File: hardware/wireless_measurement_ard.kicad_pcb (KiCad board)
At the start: 2 copper layers, 30 x 23 mm, 24 parts, among them J1 Conn_01x08, J2 Tag-Connect, SW1 SW_SPDT, U1 EFM8LB1, U2 JDY-08, U3 MCP16415, U4 MAX40204

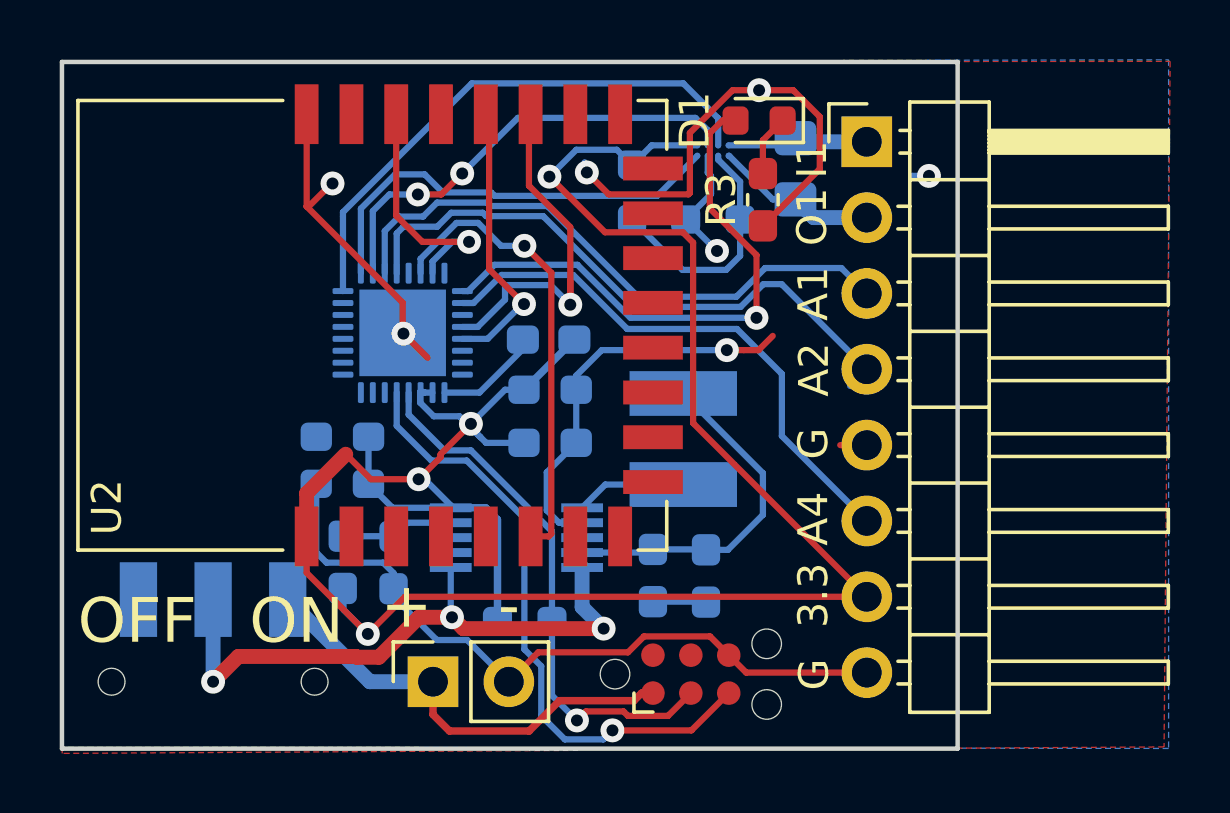
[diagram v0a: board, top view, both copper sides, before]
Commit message: critical fix for cap connectd to power instead of gnd
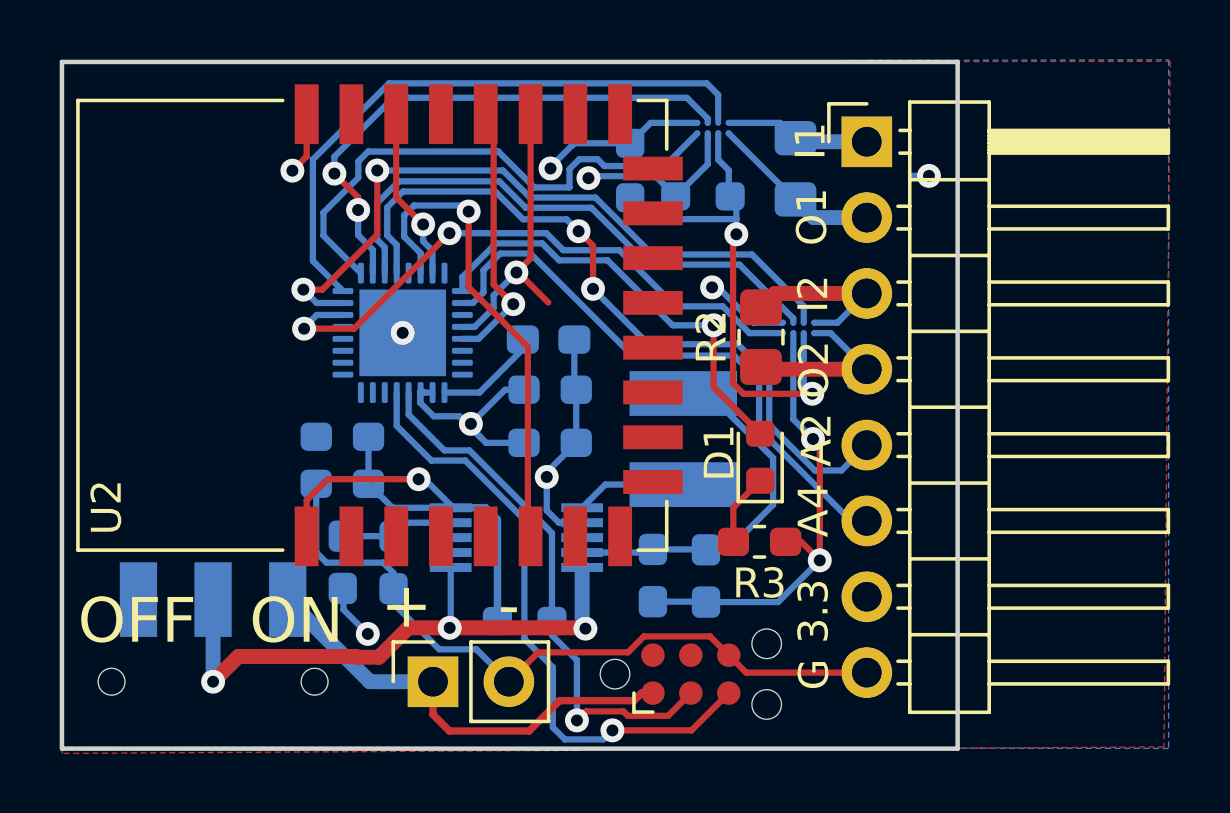
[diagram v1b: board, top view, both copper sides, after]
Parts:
- added R2: 1R, Resistor_SMD:R_0805_2012Metric_Pad1.20x1.40mm_HandSolder, F.Cu at (133.4, 84.2)
- added U5: MAX40204, ben_common:BGA-8_4x2_1.468x0.848mm, B.Cu at (134.7, 83.9)
- moved R3 11.5 mm to (133.4, 91.1), turned to 0 degrees
- moved D1 11.3 mm to (133.4, 88.2), turned to 90 degrees
- moved R8 0.84 mm to (131.5, 79.5)
- moved U4 0.75 mm to (131.8, 77.2)
- moved R7 0.73 mm to (129.0, 78.6)
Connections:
- net Net-(R7-Pad2) renamed HALF
- C7 pad 1: +3V3 -> GND
- J1 pad 3: A1 -> C2_IN
- J1 pad 4: A2 -> C2_OUT
- J1 pad 5: VHIGH -> A2
- U1 pad 14: Net-(U1-Pad14) -> MAX_SHDN2
- U1 pad 15: Net-(U1-Pad15) -> GAIN2
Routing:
- net +3V3: track 79.3 -> 35.0 mm, vias 4 -> 5
- net GAIN2: track 0.00 -> 23.6 mm, vias 0 -> 2
- net MAX_SHDN2: track 0.00 -> 20.3 mm, vias 0 -> 2
- net GND: track 71.2 -> 56.1 mm
- net HALF: track 8.17 -> 17.6 mm, vias 0 -> 2
- net C2_OUT: track 0.00 -> 6.57 mm
- net C2_IN: track 0.00 -> 5.90 mm
- net LED: track 18.8 -> 14.8 mm
- net A2: track 20.9 -> 24.7 mm, vias 0 -> 2
- net MAX_SHDN: track 14.8 -> 18.0 mm
- net A0: track 15.3 -> 18.2 mm
- net ARD_RX: track 12.5 -> 9.79 mm
- net PWRC: track 8.09 -> 5.83 mm
- net GAIN: track 18.4 -> 20.5 mm
- net STATUS: track 15.5 -> 16.8 mm
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- added copper zone on PWR, net +3V3
- added copper zone on GND, net GND
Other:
- copper layers 2 -> 4
- board text added: "I2"
- board text added: "O2"
- board text added: "SWM-mini-4 Oct 21"
- board text removed: "A1"
- board text removed: "SWM-mini-3 Oct 21"

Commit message: added logo
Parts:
- added U6: Logo, icons:icon, F.Cu at (114.8, 86.4)
- SW1: footprint Button_Switch_SMD:SW_SPDT_CK-JS102011SAQN -> ben_common:SW_SPDT_CK-JS102011SAQN

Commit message: update PCB
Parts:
- added C8: 4.7uF, Capacitor_SMD:C_0603_1608Metric_Pad1.08x0.95mm_HandSolder, F.Cu at (132.5, 77.1)
- added C9: 0.1uF, Capacitor_SMD:C_0603_1608Metric_Pad1.08x0.95mm_HandSolder, F.Cu at (132.5, 80.6)
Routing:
- net +3V3: track 35.0 -> 44.5 mm, vias 5 -> 6
- net GND: track 56.1 -> 60.2 mm, vias 7 -> 8
- net HALF: track 17.6 -> 19.1 mm

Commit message: Added capacitor
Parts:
- moved C8 0.99 mm to (133.5, 76.9)
- moved C9 0.97 mm to (133.5, 80.6)
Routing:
- net GND: track 60.2 -> 58.4 mm
- net +3V3: track 44.5 -> 46.1 mm
- net HALF: track 19.1 -> 17.6 mm

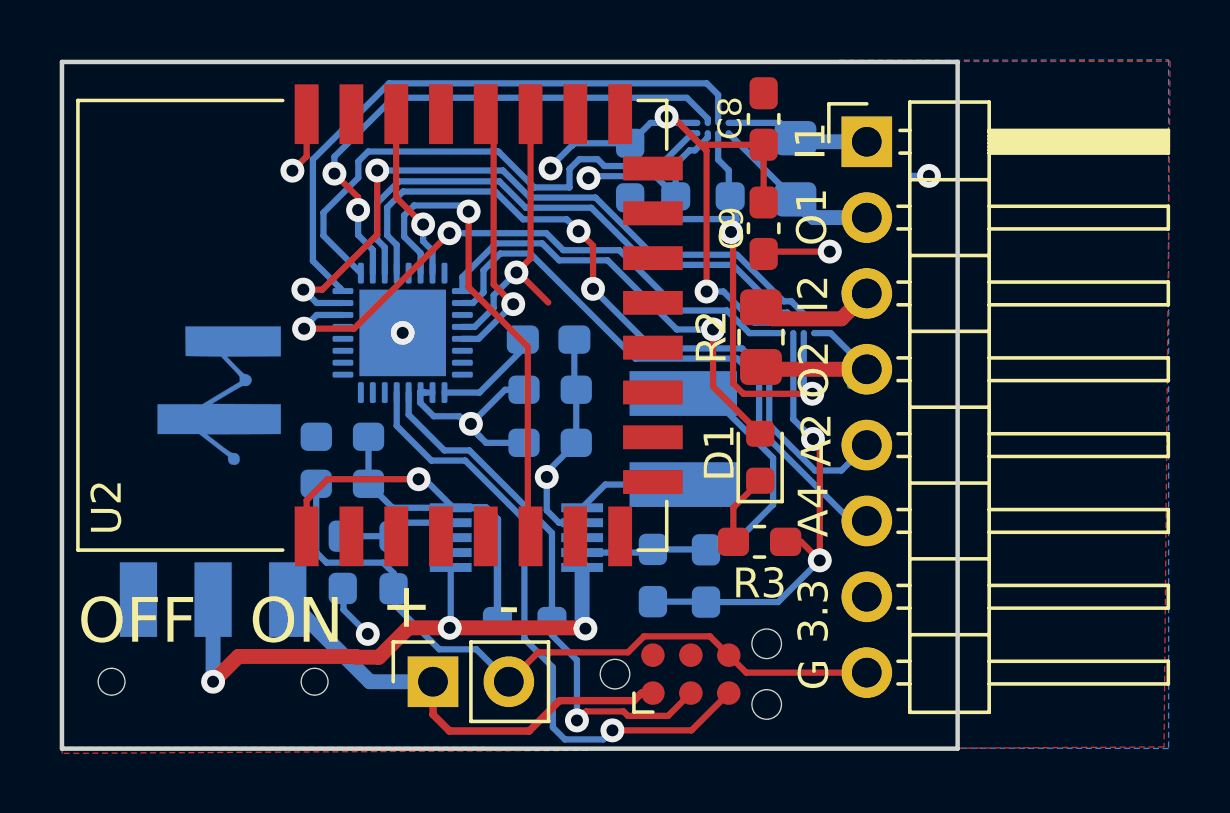
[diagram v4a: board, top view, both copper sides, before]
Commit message: added line to measure the half voltage for the MAX40204
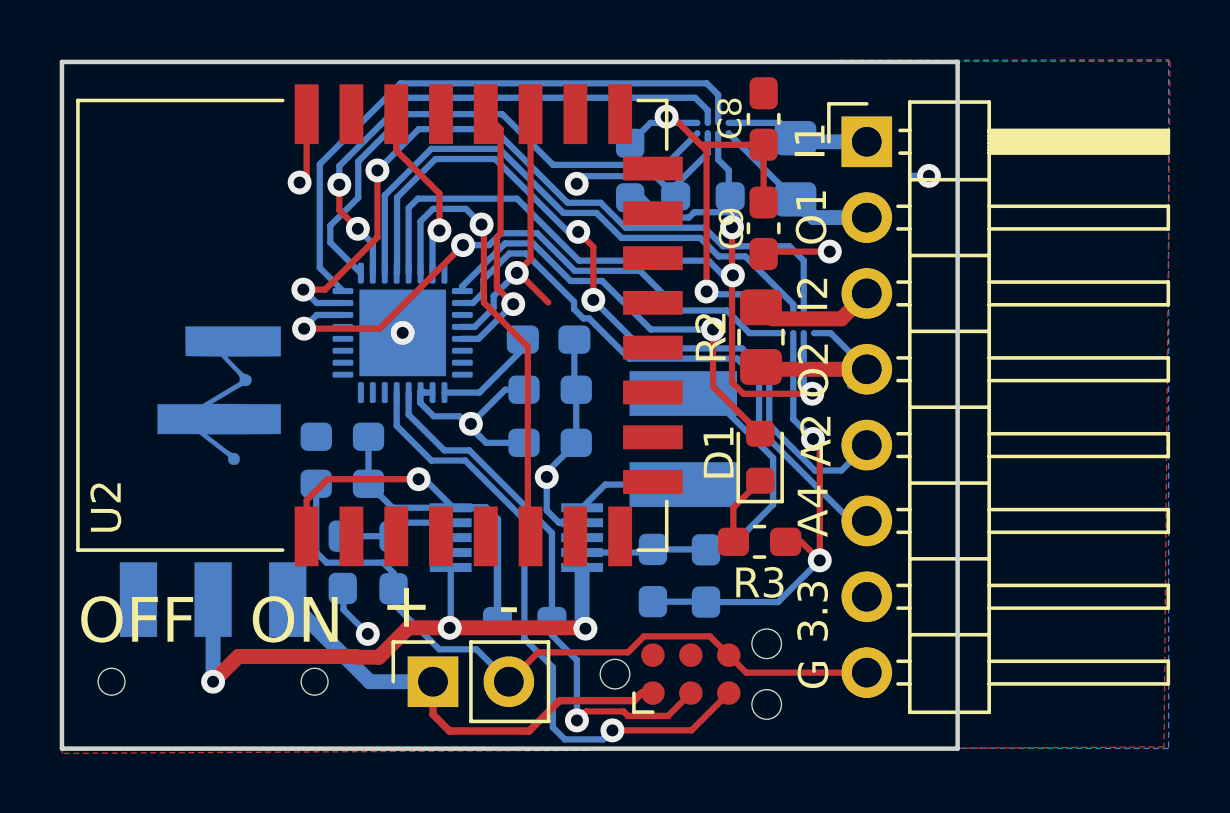
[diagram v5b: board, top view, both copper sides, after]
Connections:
- R7 pad 2: HALF -> A5
- R8 pad 1: HALF -> A5
- U1 pad 21: Net-(U1-Pad21) -> A5
- U4 pad B2: HALF -> A5
- U5 pad B2: HALF -> A5
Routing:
- net A5: track 0.00 -> 32.0 mm, vias 0 -> 3
- net HALF: track 17.6 -> 0.00 mm, vias 2 -> 0
- net +3V3: track 46.1 -> 43.2 mm, vias 6 -> 5
- net GAIN2: track 23.5 -> 25.7 mm
- net STATUS: track 16.8 -> 15.8 mm
- net A1: track 18.7 -> 19.7 mm
- net A2: track 24.7 -> 25.6 mm
- net GND: track 58.4 -> 59.1 mm
